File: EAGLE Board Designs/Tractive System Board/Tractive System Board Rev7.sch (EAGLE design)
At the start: 114 parts, among them J1 CONNECTOR-5_MICRO_V7S_, J2 CONNECTOR-5_MICRO_V6S_, J3 CONNECTOR-8_μF_T_V_BLACK, K1 RELAY_SPST_NO_D_24, Q1 TRANSISTOR_N_MOS_POWERFLAT5X6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, Q2 TRANSISTOR_N_MOS__PMV15ENEA, T1 TRANSFORMER(3W), U1 VOLTAGE_REGULATOR_SOT-223_10V, U10 LTC6994-2, U2 LT8316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

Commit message: Added text label for EN/UVLO net
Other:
- note added: "TS+FUSED > 60V EN/UVLO > 1.22V"
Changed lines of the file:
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@@
 <wire x1="5.08" y1="5.08" x2="5.08" y2="210.82" width="0.254" layer="97" style="longdash"/>
 <text x="68.58" y="187.96" size="2.54" layer="97">Precharger Power Stage</text>
+<text x="93.726" y="173.99" size="1.27" layer="95">TS+FUSED &gt; 60V
+EN/UVLO &gt; 1.22V</text>
 </plain>
 <instances>

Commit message: tsb-rev7 update
Added DNP resistor in parallel to R30 of the input to the optoisolator incase R30 is not enough.
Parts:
- added R42: RESISTOR_0603_DNP, HyTechDevices:RESISTOR_0603_DNP
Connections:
- net N$53: now also R42.2
- net SHDN: now also R42.1
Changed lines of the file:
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@@
 <part name="R40" library="HyTechDevices" deviceset="RESISTOR_?_*" device="0603" technology="41.2K"/>
 <part name="R41" library="HyTechDevices" deviceset="RESISTOR_?_*" device="0603" technology="41.2K"/>
+<part name="R42" library="HyTechDevices" deviceset="RESISTOR_?_*" device="0603" technology="DNP"/>
 </parts>
 <sheets>
@@
 <attribute name="CAPACITANCE" x="34.798" y="97.79" size="1.27" layer="96" rot="R90" align="top-center"/>
 </instance>
+<instance part="R42" gate="G$1" x="162.56" y="157.48" smashed="yes">
+<attribute name="NAME" x="161.29" y="158.75" size="1.27" layer="95" align="bottom-center"/>
+<attribute name="RESISTANCE" x="161.29" y="156.21" size="1.27" layer="96" align="top-center"/>
+</instance>
 </instances>
 <busses>
@@
 <label x="154.94" y="162.56" size="1.27" layer="95" rot="R180" xref="yes"/>
 <pinref part="R30" gate="G$1" pin="1"/>
+<wire x1="157.48" y1="162.56" x2="157.48" y2="157.48" width="0.1524" layer="91"/>
+<junction x="157.48" y="162.56"/>
+<pinref part="R42" gate="G$1" pin="1"/>
 </segment>
 <segment>
@@
 <pinref part="U5" gate="G$1" pin="CONTROL+"/>
 <pinref part="R30" gate="G$1" pin="2"/>
-</segment>
-</net>
+<wire x1="165.1" y1="162.56" x2="165.1" y2="157.48" width="0.1524" layer="91"/>
+<junction x="165.1" y="162.56"/>
+<pinref part="R42" gate="G$1" pin="2"/>
+</segment>
+</net>

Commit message: Post review update
tsb-rev7 new plans
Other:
- note added: "TS+FUSED > 60V EN/UVLO > 1.27V"
- note removed: "TS+FUSED > 60V EN/UVLO > 1.22V"
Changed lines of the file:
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@@
 <text x="68.58" y="187.96" size="2.54" layer="97">Precharger Power Stage</text>
 <text x="93.726" y="173.99" size="1.27" layer="95">TS+FUSED &gt; 60V
-EN/UVLO &gt; 1.22V</text>
+EN/UVLO &gt; 1.27V</text>
 </plain>
 <instances>
@@
 <pinref part="C6" gate="G$1" pin="2"/>
 <wire x1="91.44" y1="142.24" x2="91.44" y2="133.35" width="0.6096" layer="91"/>
-<pinref part="R40" gate="G$1" pin="1"/>
 <pinref part="R41" gate="G$1" pin="1"/>
-<wire x1="76.2" y1="142.24" x2="83.82" y2="142.24" width="0.6096" layer="91"/>
 <wire x1="83.82" y1="142.24" x2="83.82" y2="133.35" width="0.6096" layer="91"/>
-<junction x="83.82" y="142.24"/>
 <wire x1="83.82" y1="133.35" x2="91.44" y2="133.35" width="0.6096" layer="91"/>
 <junction x="83.82" y="133.35"/>
 <junction x="91.44" y="133.35"/>
+<pinref part="R40" gate="G$1" pin="1"/>
+<wire x1="83.82" y1="142.24" x2="76.2" y2="142.24" width="0.6096" layer="91"/>
+<junction x="83.82" y="142.24"/>
 </segment>
 <segment>
@@
 <wire x1="83.82" y1="172.72" x2="83.82" y2="149.86" width="0.6096" layer="91"/>
 <junction x="83.82" y="172.72"/>
+<pinref part="R41" gate="G$1" pin="2"/>
+<pinref part="U2" gate="G$1" pin="EN/UVLO"/>
+<pinref part="R40" gate="G$1" pin="2"/>
 <wire x1="83.82" y1="149.86" x2="76.2" y2="149.86" width="0.6096" layer="91"/>
-<pinref part="R40" gate="G$1" pin="2"/>
-<pinref part="R41" gate="G$1" pin="2"/>
 <junction x="83.82" y="149.86"/>
-<pinref part="U2" gate="G$1" pin="EN/UVLO"/>
-</segment>
-</net>
+</segment>
+</net>

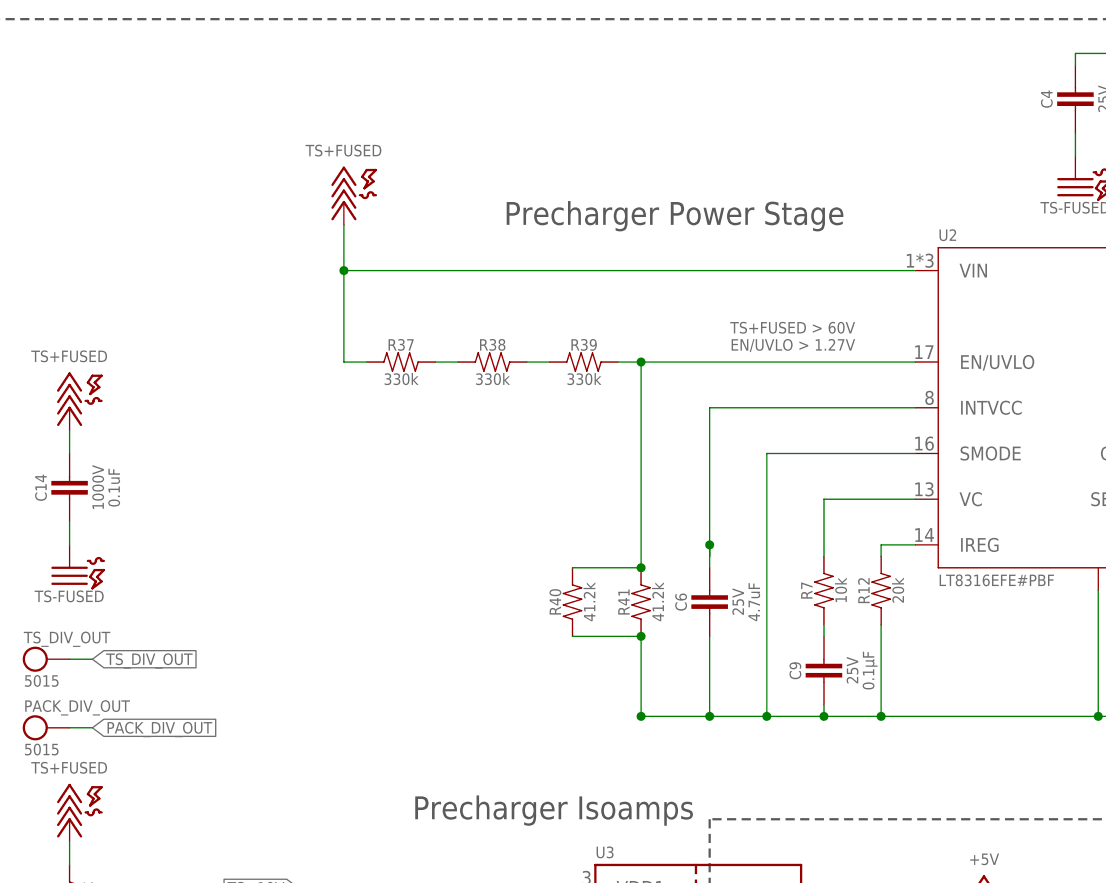
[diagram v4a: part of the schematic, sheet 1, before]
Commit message: tsb-rev7 update
Updated voltage divider and added bypass capacitors to EN/UVLO pin on the flyback controller
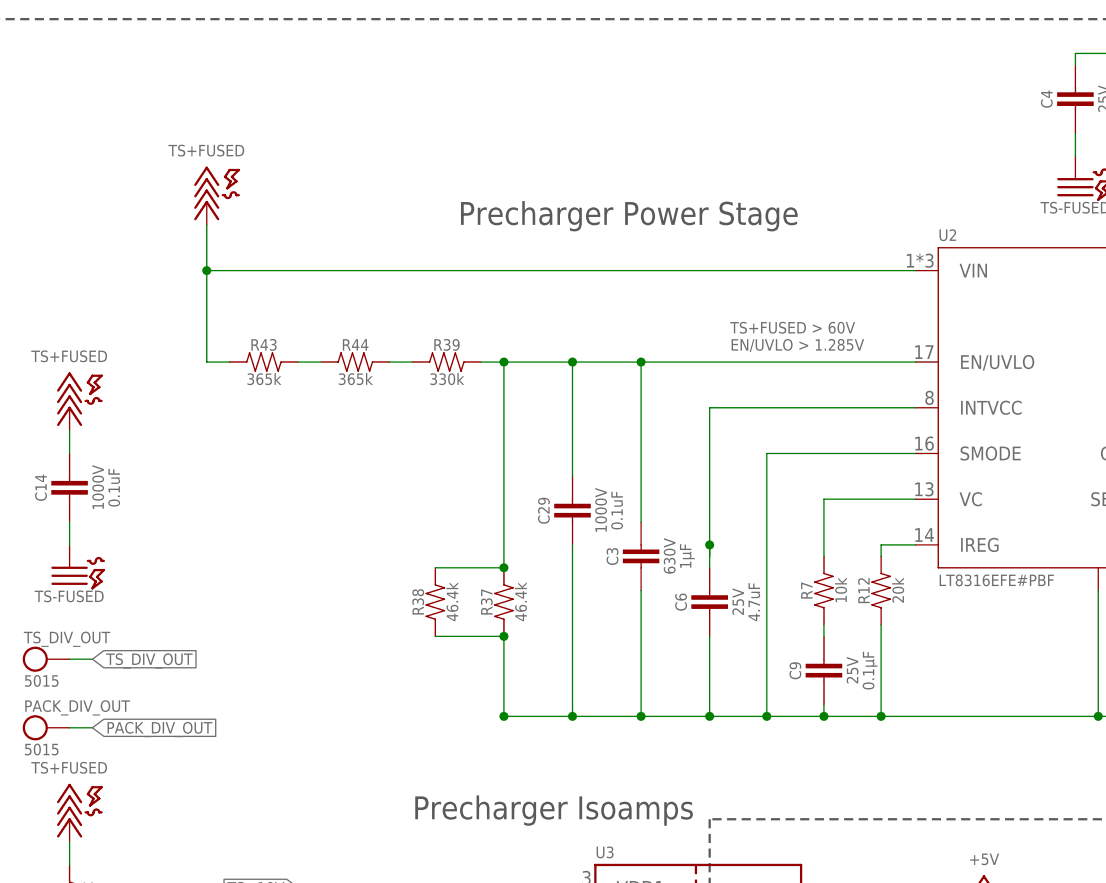
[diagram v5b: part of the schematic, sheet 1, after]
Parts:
- removed R40, R41: RESISTOR_0603_41.2K, HyTechDevices:RESISTOR_0603_41.2K
- added C29: CAPACITOR_1812_1000V_0.1UF, HyTechDevices:CAPACITOR_1812_1000V_0.1UF
- added C3: CAPACITOR_2220_630V_1UF, HyTechDevices:CAPACITOR_2220_630V_1UF
- added R43, R44: RESISTOR_0805_HV365K, HyTechDevices:RESISTOR_0805_HV365K
- R37, R38: value RESISTOR_0805_HV330K -> RESISTOR_1206_HV46.4K; device HyTechDevices:RESISTOR_0805_HV330K -> HyTechDevices:RESISTOR_1206_HV46.4K
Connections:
- net N$29: now also R43.2, R44.1; no longer R37.2, R38.1
- net N$31: now also R44.2; no longer R38.2
- net N$32: now also C29.1, C3.1, R37.2, R38.2; no longer R40.2, R41.2
- net TS+FUSED: now also R43.1; no longer R37.1
- net TS-FUSED: now also C29.2, C3.2, R37.1, R38.1; no longer R40.1, R41.1
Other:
- note added: "TS+FUSED > 60V EN/UVLO > 1.285V"
- note removed: "TS+FUSED > 60V EN/UVLO > 1.27V"
- moved on the sheet: R37, R38, R39

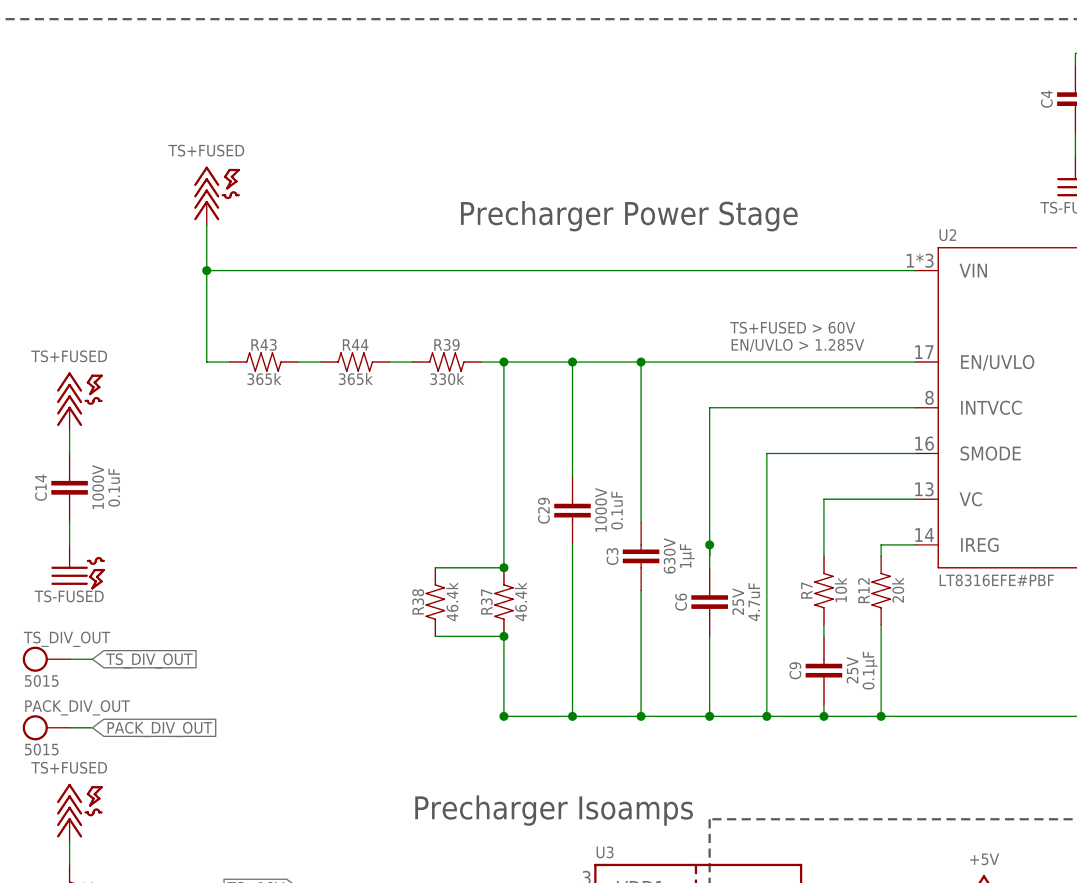
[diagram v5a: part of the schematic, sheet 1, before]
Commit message: tsb-rev7 update
Removed 1uF bypass capacitor to EN/UVLO input of flyback controller
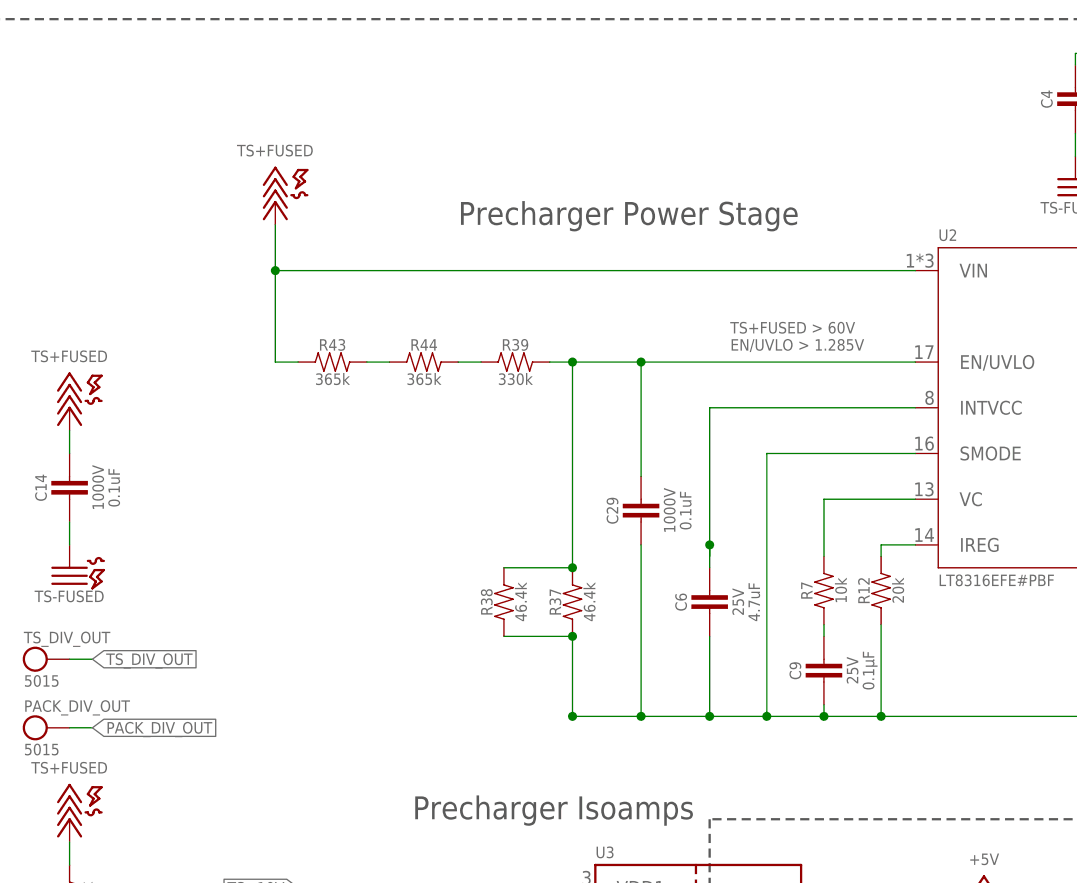
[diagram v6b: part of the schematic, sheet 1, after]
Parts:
- removed C3: CAPACITOR_2220_630V_1UF, HyTechDevices:CAPACITOR_2220_630V_1UF
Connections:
- net N$32: no longer C3.1
- net TS-FUSED: no longer C3.2
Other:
- moved on the sheet: C29, R37, R38, R39, R43, R44
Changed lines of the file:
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@@
 <part name="R37" library="HyTechDevices" deviceset="RESISTOR_?_*" device="1206" technology="HV46.4K"/>
 <part name="R38" library="HyTechDevices" deviceset="RESISTOR_?_*" device="1206" technology="HV46.4K"/>
-<part name="C3" library="HyTechDevices" deviceset="CAPACITOR_?_*" device="2220" technology="630V_1UF"/>
 <part name="C29" library="HyTechDevices" deviceset="CAPACITOR_?_*" device="1812" technology="1000V_0.1UF"/>
 </parts>
@@
 <attribute name="CAPACITANCE" x="244.856" y="172.72" size="1.27" layer="96" rot="R270" align="top-center"/>
 </instance>
-<instance part="U$5" gate="G$1" x="35.56" y="190.5" smashed="yes">
-<attribute name="VALUE" x="35.56" y="195.58" size="1.27" layer="96" align="bottom-center"/>
-</instance>
-<instance part="R39" gate="G$1" x="63.5" y="172.72" smashed="yes">
-<attribute name="NAME" x="62.23" y="173.99" size="1.27" layer="95" align="bottom-center"/>
-<attribute name="RESISTANCE" x="62.23" y="171.45" size="1.27" layer="96" align="top-center"/>
-</instance>
-<instance part="R43" gate="G$1" x="43.18" y="172.72" smashed="yes">
-<attribute name="NAME" x="41.91" y="173.99" size="1.27" layer="95" align="bottom-center"/>
-<attribute name="RESISTANCE" x="41.91" y="171.45" size="1.27" layer="96" align="top-center"/>
-</instance>
-<instance part="R44" gate="G$1" x="53.34" y="172.72" smashed="yes">
-<attribute name="NAME" x="52.07" y="173.99" size="1.27" layer="95" align="bottom-center"/>
-<attribute name="RESISTANCE" x="52.07" y="171.45" size="1.27" layer="96" align="top-center"/>
-</instance>
-<instance part="R37" gate="G$1" x="68.58" y="147.32" smashed="yes" rot="R90">
+<instance part="U$5" gate="G$1" x="43.18" y="190.5" smashed="yes">
+<attribute name="VALUE" x="43.18" y="195.58" size="1.27" layer="96" align="bottom-center"/>
+</instance>
+<instance part="R39" gate="G$1" x="71.12" y="172.72" smashed="yes">
+<attribute name="NAME" x="69.85" y="173.99" size="1.27" layer="95" align="bottom-center"/>
+<attribute name="RESISTANCE" x="69.85" y="171.45" size="1.27" layer="96" align="top-center"/>
+</instance>
+<instance part="R43" gate="G$1" x="50.8" y="172.72" smashed="yes">
+<attribute name="NAME" x="49.53" y="173.99" size="1.27" layer="95" align="bottom-center"/>
+<attribute name="RESISTANCE" x="49.53" y="171.45" size="1.27" layer="96" align="top-center"/>
+</instance>
+<instance part="R44" gate="G$1" x="60.96" y="172.72" smashed="yes">
+<attribute name="NAME" x="59.69" y="173.99" size="1.27" layer="95" align="bottom-center"/>
+<attribute name="RESISTANCE" x="59.69" y="171.45" size="1.27" layer="96" align="top-center"/>
+</instance>
+<instance part="R37" gate="G$1" x="76.2" y="147.32" smashed="yes" rot="R90">
+<attribute name="NAME" x="74.93" y="146.05" size="1.27" layer="95" rot="R90" align="bottom-center"/>
+<attribute name="RESISTANCE" x="77.47" y="146.05" size="1.27" layer="96" rot="R90" align="top-center"/>
+</instance>
+<instance part="R38" gate="G$1" x="68.58" y="147.32" smashed="yes" rot="R90">
 <attribute name="NAME" x="67.31" y="146.05" size="1.27" layer="95" rot="R90" align="bottom-center"/>
 <attribute name="RESISTANCE" x="69.85" y="146.05" size="1.27" layer="96" rot="R90" align="top-center"/>
 </instance>
-<instance part="R38" gate="G$1" x="60.96" y="147.32" smashed="yes" rot="R90">
-<attribute name="NAME" x="59.69" y="146.05" size="1.27" layer="95" rot="R90" align="bottom-center"/>
-<attribute name="RESISTANCE" x="62.23" y="146.05" size="1.27" layer="96" rot="R90" align="top-center"/>
-</instance>
-<instance part="C3" gate="G$1" x="83.82" y="152.4" smashed="yes" rot="R90">
-<attribute name="NAME" x="81.28" y="151.13" size="1.27" layer="95" rot="R90" align="bottom-center"/>
-<attribute name="VOLTAGE" x="86.36" y="151.13" size="1.27" layer="96" rot="R90" align="top-center"/>
-<attribute name="CAPACITANCE" x="88.138" y="151.13" size="1.27" layer="96" rot="R90" align="top-center"/>
-</instance>
-<instance part="C29" gate="G$1" x="76.2" y="157.48" smashed="yes" rot="R90">
-<attribute name="NAME" x="73.66" y="156.21" size="1.27" layer="95" rot="R90" align="bottom-center"/>
-<attribute name="VOLTAGE" x="78.74" y="156.21" size="1.27" layer="96" rot="R90" align="top-center"/>
-<attribute name="CAPACITANCE" x="80.518" y="156.21" size="1.27" layer="96" rot="R90" align="top-center"/>
+<instance part="C29" gate="G$1" x="83.82" y="157.48" smashed="yes" rot="R90">
+<attribute name="NAME" x="81.28" y="156.21" size="1.27" layer="95" rot="R90" align="bottom-center"/>
+<attribute name="VOLTAGE" x="86.36" y="156.21" size="1.27" layer="96" rot="R90" align="top-center"/>
+<attribute name="CAPACITANCE" x="88.138" y="156.21" size="1.27" layer="96" rot="R90" align="top-center"/>
 </instance>
 </instances>
@@
 <pinref part="C6" gate="G$1" pin="2"/>
 <wire x1="91.44" y1="142.24" x2="91.44" y2="133.35" width="0.6096" layer="91"/>
-<wire x1="68.58" y1="142.24" x2="68.58" y2="133.35" width="0.6096" layer="91"/>
-<wire x1="68.58" y1="133.35" x2="76.2" y2="133.35" width="0.6096" layer="91"/>
-<junction x="68.58" y="133.35"/>
+<wire x1="76.2" y1="142.24" x2="76.2" y2="133.35" width="0.6096" layer="91"/>
+<wire x1="76.2" y1="133.35" x2="83.82" y2="133.35" width="0.6096" layer="91"/>
+<junction x="76.2" y="133.35"/>
 <junction x="91.44" y="133.35"/>
 <pinref part="R37" gate="G$1" pin="1"/>
 <pinref part="R38" gate="G$1" pin="1"/>
-<wire x1="76.2" y1="133.35" x2="83.82" y2="133.35" width="0.6096" layer="91"/>
 <wire x1="83.82" y1="133.35" x2="91.44" y2="133.35" width="0.6096" layer="91"/>
-<wire x1="68.58" y1="142.24" x2="60.96" y2="142.24" width="0.6096" layer="91"/>
-<junction x="68.58" y="142.24"/>
+<wire x1="76.2" y1="142.24" x2="68.58" y2="142.24" width="0.6096" layer="91"/>
+<junction x="76.2" y="142.24"/>
 <pinref part="C29" gate="G$1" pin="2"/>
-<wire x1="76.2" y1="152.4" x2="76.2" y2="133.35" width="0.6096" layer="91"/>
-<junction x="76.2" y="133.35"/>
-<pinref part="C3" gate="G$1" pin="2"/>
-<wire x1="83.82" y1="147.32" x2="83.82" y2="133.35" width="0.6096" layer="91"/>
+<wire x1="83.82" y1="152.4" x2="83.82" y2="133.35" width="0.6096" layer="91"/>
 <junction x="83.82" y="133.35"/>
 </segment>
@@
 <segment>
 <pinref part="U$5" gate="G$1" pin="TS+FUSED"/>
-<wire x1="35.56" y1="187.96" x2="35.56" y2="182.88" width="0.6096" layer="91"/>
-<wire x1="35.56" y1="182.88" x2="35.56" y2="172.72" width="0.6096" layer="91"/>
+<wire x1="43.18" y1="187.96" x2="43.18" y2="182.88" width="0.6096" layer="91"/>
+<wire x1="43.18" y1="182.88" x2="43.18" y2="172.72" width="0.6096" layer="91"/>
 <pinref part="U2" gate="G$1" pin="VIN"/>
-<wire x1="35.56" y1="182.88" x2="114.3" y2="182.88" width="0.6096" layer="91"/>
-<junction x="35.56" y="182.88"/>
+<wire x1="43.18" y1="182.88" x2="114.3" y2="182.88" width="0.6096" layer="91"/>
+<junction x="43.18" y="182.88"/>
 <pinref part="R43" gate="G$1" pin="1"/>
-<wire x1="38.1" y1="172.72" x2="35.56" y2="172.72" width="0.6096" layer="91"/>
+<wire x1="45.72" y1="172.72" x2="43.18" y2="172.72" width="0.6096" layer="91"/>
 </segment>
 </net>
@@
 <net name="N$32" class="0">
 <segment>
-<wire x1="68.58" y1="172.72" x2="76.2" y2="172.72" width="0.6096" layer="91"/>
 <wire x1="76.2" y1="172.72" x2="83.82" y2="172.72" width="0.6096" layer="91"/>
 <wire x1="83.82" y1="172.72" x2="114.3" y2="172.72" width="0.6096" layer="91"/>
-<wire x1="68.58" y1="172.72" x2="68.58" y2="149.86" width="0.6096" layer="91"/>
+<wire x1="76.2" y1="172.72" x2="76.2" y2="149.86" width="0.6096" layer="91"/>
 <pinref part="U2" gate="G$1" pin="EN/UVLO"/>
 <pinref part="R39" gate="G$1" pin="2"/>
-<wire x1="66.04" y1="172.72" x2="68.58" y2="172.72" width="0.6096" layer="91"/>
-<junction x="68.58" y="172.72"/>
+<wire x1="73.66" y1="172.72" x2="76.2" y2="172.72" width="0.6096" layer="91"/>
+<junction x="76.2" y="172.72"/>
 <pinref part="R37" gate="G$1" pin="2"/>
 <pinref part="R38" gate="G$1" pin="2"/>
-<wire x1="68.58" y1="149.86" x2="60.96" y2="149.86" width="0.6096" layer="91"/>
-<junction x="68.58" y="149.86"/>
+<wire x1="76.2" y1="149.86" x2="68.58" y2="149.86" width="0.6096" layer="91"/>
+<junction x="76.2" y="149.86"/>
 <pinref part="C29" gate="G$1" pin="1"/>
-<wire x1="76.2" y1="172.72" x2="76.2" y2="160.02" width="0.6096" layer="91"/>
-<junction x="76.2" y="172.72"/>
-<pinref part="C3" gate="G$1" pin="1"/>
-<wire x1="83.82" y1="154.94" x2="83.82" y2="172.72" width="0.6096" layer="91"/>
-<wire x1="83.82" y1="172.974" x2="83.82" y2="172.72" width="0.1524" layer="91"/>
+<wire x1="83.82" y1="172.72" x2="83.82" y2="160.02" width="0.6096" layer="91"/>
 <junction x="83.82" y="172.72"/>
 </segment>
@@
 <pinref part="R43" gate="G$1" pin="2"/>
 <pinref part="R44" gate="G$1" pin="1"/>
-<wire x1="45.72" y1="172.72" x2="48.26" y2="172.72" width="0.6096" layer="91"/>
+<wire x1="53.34" y1="172.72" x2="55.88" y2="172.72" width="0.6096" layer="91"/>
 </segment>
 </net>
@@
 <pinref part="R44" gate="G$1" pin="2"/>
 <pinref part="R39" gate="G$1" pin="1"/>
-<wire x1="55.88" y1="172.72" x2="58.42" y2="172.72" width="0.6096" layer="91"/>
-</segment>
-</net>
+<wire x1="63.5" y1="172.72" x2="66.04" y2="172.72" width="0.6096" layer="91"/>
+</segment>
+</net>
